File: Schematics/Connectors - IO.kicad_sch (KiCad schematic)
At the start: 5 parts, among them J1203 JST_XH_B5B

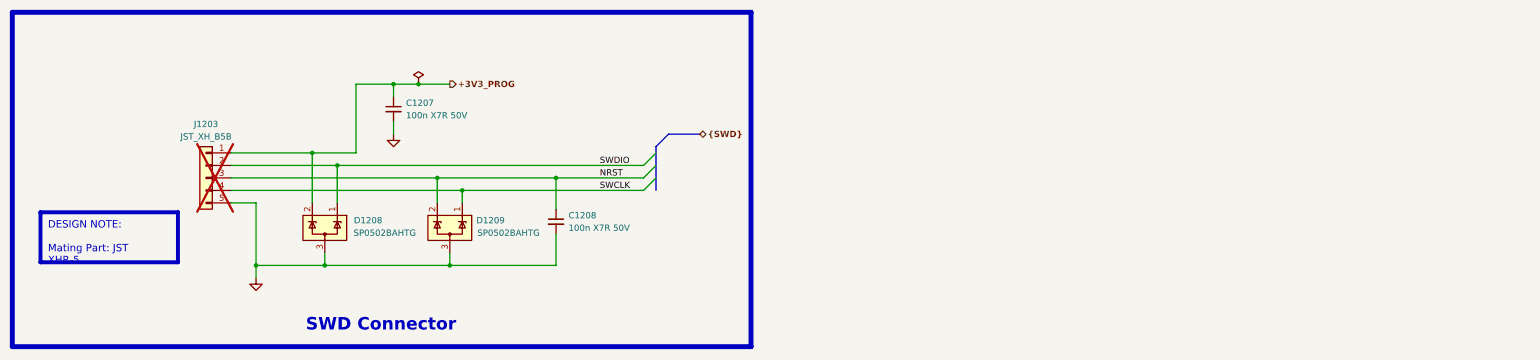
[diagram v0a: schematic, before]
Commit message: Add external Power connector and Power conversion & Selection ckt
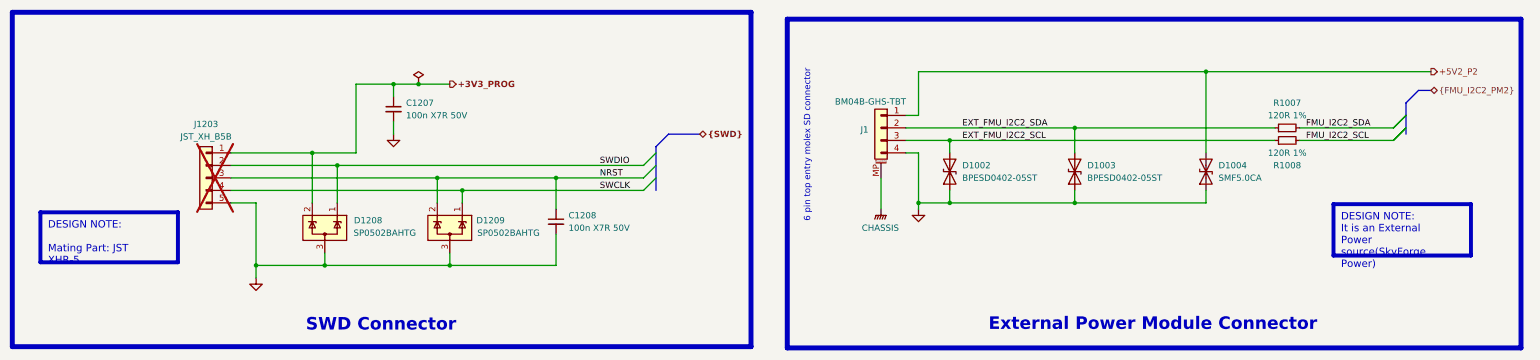
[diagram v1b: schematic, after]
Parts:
- added D1002, D1003: BPESD0402-05ST, Diode_SMD:D_0402_1005Metric, symbol Device:D_TVS
- added D1004: SMF5.0CA, Diode_SMD:D_SOD-123F, symbol Device:D_TVS
- added J1: BM04B-GHS-TBT, Connector_JST:JST_GH_BM04B-GHS-TBT_1x04-1MP_P1.25mm_Vertical, symbol Connector_Generic_MountingPin:Conn_01x04_MountingPin
- added R1007, R1008: 120R 1%, Resistor_SMD:R_0402_1005Metric, symbol Device:R_Small
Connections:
- net GND: now also D1002.1 (A1), D1003.1 (A1), D1004.1 (A1), J1.4 (Pin_4)
- new net +5V2_P2: D1004.2 (A2), J1.1 (Pin_1)
- new net CHASSIS: J1.MP (MountPin)
- new net EXT_FMU_I2C2_SCL: D1002.2 (A2), J1.3 (Pin_3), R1008.1
- new net EXT_FMU_I2C2_SDA: D1003.2 (A2), J1.2 (Pin_2), R1007.1
- new net FMU_I2C2_SCL: R1008.2
- new net FMU_I2C2_SDA: R1007.2
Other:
- note added: "6 pin top entry molex SD connector"

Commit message: Add USB
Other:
- note added: "4 pin top entry molex SD connector"
- note removed: "6 pin top entry molex SD connector"
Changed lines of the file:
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@@
 		)
 	)
-	(text "6 pin top entry molex SD connector"
+	(text "4 pin top entry molex SD connector"
 		(exclude_from_sim no)
 		(at 185.674 162.306 90)
